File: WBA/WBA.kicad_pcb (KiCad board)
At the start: 4 copper layers, 123.2 x 75.2 mm, 142 parts, among them J1 Signal input, J10 Conn_01x02, J11 Conn_01x02, J12 Conn_01x02, J13 Conn_01x02, J14 Conn_01x02, J15 Conn_01x02, J16 LPF_potentiometer_100k, J17 Amp Selector, J19 Detector Input, J2 Conn_01x24, J3 Conn_01x04, J4 Conn_01x24, J5 Input Power, J6 Conn_01x04, J7 Conn_01x04, J8 Conn_01x02, J9 Conn_01x02, Q1 A03400A, Q2 A03401A, U11 MAX7424EUA+T, U12 TL072, U14 L7805, U15 L7905, U16 TPS5430DDA, U19 TLV2374IDR, U2 TLV2372, U20 TLV2374IDR, U21 OP07BRZ, U22 OP07BRZ, U23 INA128, U24 INA128, U3 MAX7424EUA+T, U8 L7805

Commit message: rework of power, output wried up
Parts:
- moved C81 60.9 mm to (214.4, 56.9), turned to 180 degrees
- moved U14 57.7 mm to (212.3, 49.8), turned to 90 degrees
- moved C54 52.8 mm to (210.3, 56.9), turned to 0 degrees
- moved C73 34.7 mm to (214.8, 66.3)
- moved C82 34.7 mm to (214.8, 61.7)
- moved U15 34.7 mm to (203.4, 65.0)
- moved R42 20.6 mm to (151.3, 64.2), turned to -90 degrees
- moved R41 17.6 mm to (152.8, 64.2)
- moved C57 15.7 mm to (152.8, 67.2), turned to -90 degrees
- moved C6 14.2 mm to (202.7, 54.6)
- moved R40 9.42 mm to (198.0, 54.6), turned to -90 degrees
- moved J16 9.22 mm to (155.3, 66.1)
- moved R38 8.83 mm to (182.5, 42.3), turned to -90 degrees
- moved D2 7.20 mm to (184.8, 39.1)
- moved C41 7.13 mm to (155.8, 84.8), turned to 180 degrees
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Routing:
- net -15V: track 20.4 -> 97.9 mm
- net +5V_{display}: track 10.4 -> 81.9 mm, vias 1 -> 2
- net +5V_{detector}: track 92.5 -> 36.4 mm, vias 1 -> 0
- net Net-(J11-Pin_1): track 3.49 -> 50.5 mm, vias 0 -> 2
- net Net-(J6-Pin_1): track 3.51 -> 43.4 mm, vias 0 -> 2
- net Net-(D1-K): track 84.9 -> 124.4 mm, vias 2 -> 4
- net Net-(J10-Pin_1): track 3.39 -> 39.2 mm
- net Net-(J12-Pin_1): track 3.49 -> 38.8 mm
- net Net-(J3-Pin_1): track 3.67 -> 37.7 mm
- net -5V_{detector}: track 73.5 -> 40.1 mm
- net Net-(J13-Pin_1): track 1.27 -> 29.9 mm, vias 0 -> 2
- net Net-(J14-Pin_1): track 1.27 -> 21.0 mm
- net Net-(J15-Pin_1): track 1.27 -> 20.1 mm
- net /LPF_pot: track 23.9 -> 5.83 mm
- net Net-(D2-A): track 41.0 -> 55.1 mm
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- removed copper zone on In2.Cu, net -15V

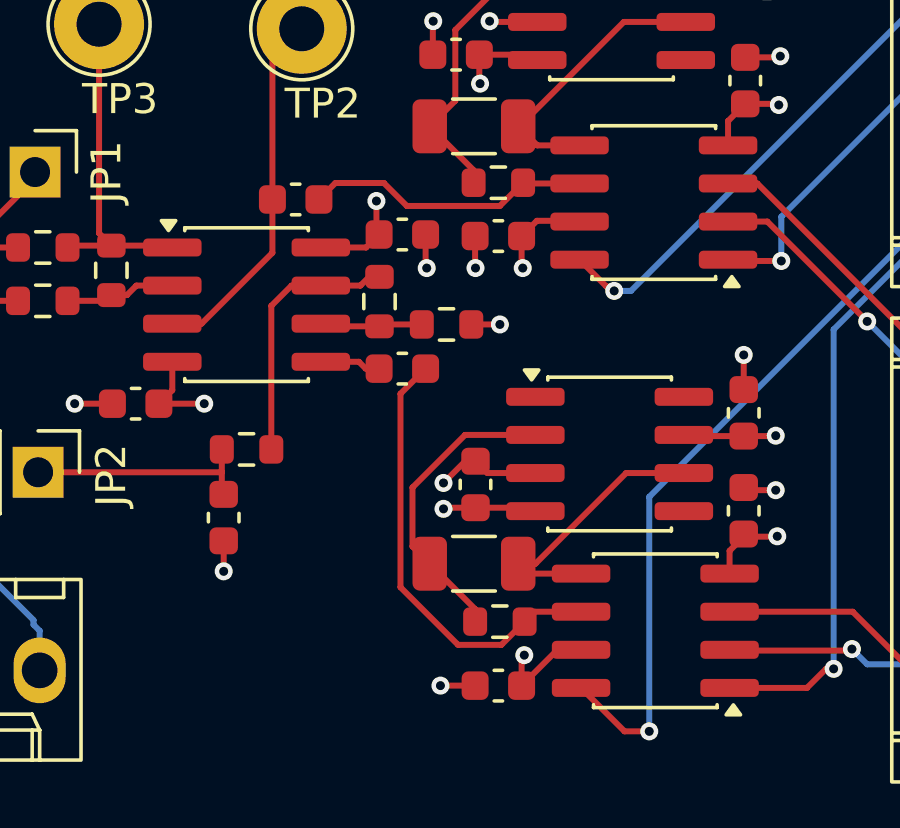
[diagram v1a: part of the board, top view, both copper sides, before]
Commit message: removed bendy paths
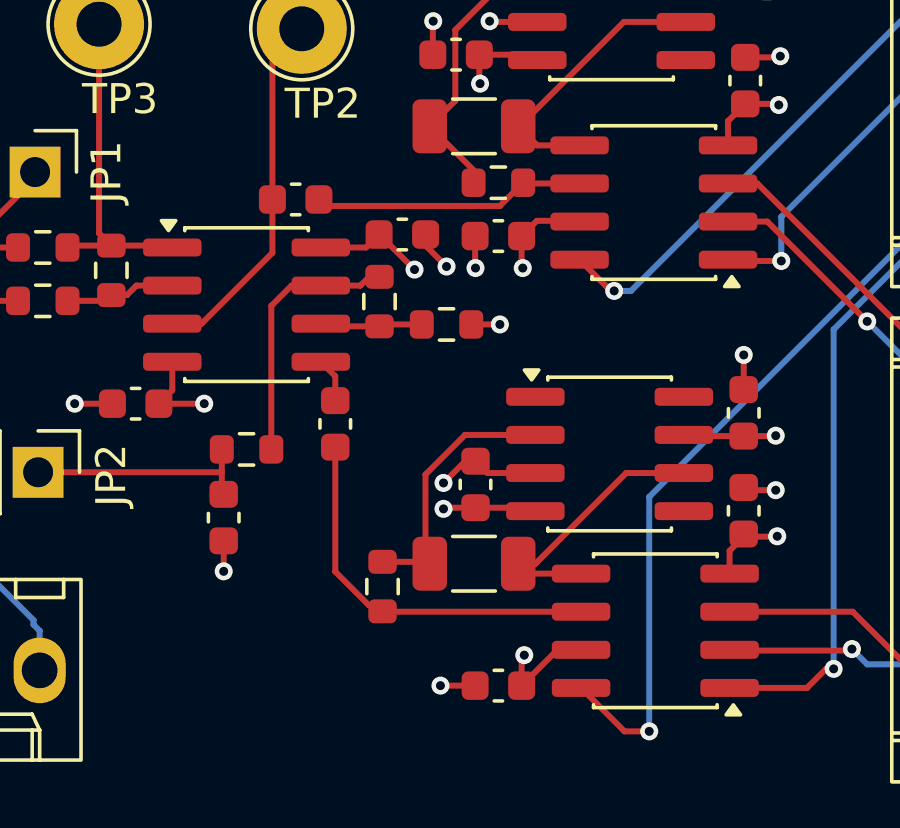
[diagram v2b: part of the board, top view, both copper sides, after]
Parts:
- moved R50 4.08 mm to (194.9, 96.8), turned to -90 degrees
- moved C62 2.90 mm to (193.3, 91.4), turned to -90 degrees
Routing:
- net Net-(C62-Pad2): track 14.9 -> 12.9 mm
- net Net-(U22--): track 10.2 -> 9.11 mm
- net Net-(U12B-+): track 2.04 -> 1.50 mm
- net +15V: track 23.8 -> 24.3 mm

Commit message: design submitted to jlc
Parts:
- removed TP2: TestPoint0, TestPoint:TestPoint_Loop_D2.54mm_Drill1.5mm_Beaded
- removed TP3: TestPoint1, TestPoint:TestPoint_Loop_D2.54mm_Drill1.5mm_Beaded
- removed U11: MAX7424EUA+T, Package_SO:MSOP-8_3x3mm_P0.65mm
- added REF**: MountingHole_3mm, MountingHole:MountingHole_3mm, F.Cu at (224.5, 100.6)
- added REF**: MountingHole_3mm, MountingHole:MountingHole_3mm, F.Cu at (95.0, 100.6)
- added REF**: MountingHole_3mm, MountingHole:MountingHole_3mm, F.Cu at (224.5, 34.5)
- added REF**: MountingHole_3mm, MountingHole:MountingHole_3mm, F.Cu at (95.0, 34.5)
- added U4: MAX7414xUA, Package_SO:MSOP-8_3x3mm_P0.65mm, F.Cu at (161.5, 87.6)
- C30: value 0.01uF -> 10nF
- U3: value MAX7424EUA+T -> MAX7414xUA
- moved U3 7.12 mm to (161.8, 93.4)
- moved C44 5.72 mm to (154.8, 83.0)
- moved C3 4.62 mm to (167.8, 95.7)
- moved C40 3.83 mm to (163.3, 84.9)
- moved C41 3.83 mm to (159.7, 84.9)
- moved C43 3.83 mm to (163.6, 90.7)
- moved C42 3.83 mm to (159.9, 90.7)
- moved C45 3.64 mm to (154.8, 87.4)
- moved R34 3.64 mm to (154.8, 84.4)
- moved R35 3.64 mm to (154.8, 88.8)
- moved C1 3.27 mm to (166.4, 90.0)
- moved R6 3.10 mm to (168.6, 93.5)
- moved C28 2.54 mm to (160.2, 39.6)
- moved R42 2.54 mm to (153.8, 64.2)
- moved C29 2.54 mm to (156.1, 39.6)
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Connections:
- C1 pad 1: Net-(U3-IN) -> Net-(U4-IN)
- C3 pad 1: Net-(U11-IN) -> Net-(U3-IN)
- C41 pad 1: Net-(U3-COM) -> Net-(U4-COM)
- C42 pad 1: Net-(U11-COM) -> Net-(U3-COM)
- R3 pad 1: Net-(U3-IN) -> Net-(U4-IN)
- R34 pad 2: Net-(U3-OUT) -> Net-(U4-OUT)
- R35 pad 2: Net-(U11-OUT) -> Net-(U3-OUT)
- R6 pad 1: Net-(U11-IN) -> Net-(U3-IN)
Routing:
- net Net-(U4-COM): track 0.00 -> 7.70 mm
- net Net-(R43-Pad2): track 11.1 -> 3.55 mm
- net Net-(U11-COM): track 7.27 -> 0.00 mm
- net Net-(D1-K): track 124.4 -> 117.2 mm
- net Net-(U12A-+): track 12.2 -> 6.09 mm
- net Net-(U11-IN): track 4.88 -> 0.00 mm
- net Net-(U4-OUT): track 0.00 -> 4.74 mm
- net Net-(U4-IN): track 0.00 -> 4.65 mm
- net Net-(U11-OUT): track 3.97 -> 0.00 mm
- net Net-(R6-Pad2): track 14.4 -> 11.2 mm
- net /L ADCin: track 21.2 -> 18.2 mm
- net Net-(U3-OUT): track 3.33 -> 5.77 mm
- net +3.3V: track 22.4 -> 24.8 mm, vias 8 -> 10
- net /R ADCin: track 21.6 -> 20.1 mm
- net Net-(J4-Pin_21): track 17.2 -> 16.1 mm
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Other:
- board size 123.2 x 75.2 mm -> 139.7 x 76.2 mm
- board text added: "+15/-15V Input"
- board text added: "AMP_L"
- board text added: "AMP_R"
- board text added: "Bypass Signal Input"
- board text added: "DIFF"
- board text added: "Detector Input"
- board text added: "FLIP_L"
- board text added: "FLIP_R"
- board text added: "FREQ"
- board text added: "Gain Selector"
- board text added: "LPF Pot"
- board text added: "SUM"
- board text added: "SYNC"
